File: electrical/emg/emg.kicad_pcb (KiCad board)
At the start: 2 copper layers, 257 parts, among them J1 USB_B, J10 Ref, J11 E2, J12 E1, J13 T1, J14 T2, J15 E2, J16 E1, J17 T1, J18 T2, J19 E2, J2 swd, J20 E1, J21 T1, J22 T2, J23 E2, J24 E1, J25 T1, J26 T2, J27 E2, J28 E1, J29 T1, J3 T3, J30 T2, J31 E2, J32 E1, J33 T1, J34 T2, J35 E2, J36 E1, J37 T1, J38 T2, J4 T3, J5 T3, J6 T3, J7 T3, J8 T3, J9 T3, P1 ~rst~, P2 bootldr, U1 stm32f405rgt6, U10 TSZ124IPT, U11 TSZ124IPT, U12 TSZ124IPT, U13 TSZ124IPT, U2 crystal-4pin, U3 my-NCP1117ST50T3G, U4 my-NCP1117ST50T3G, U5 TSV734IPT, U6 TSV734IPT, U7 TSZ124IPT, U8 TSZ124IPT, U9 TSZ124IPT

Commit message: a
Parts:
- moved R49 172.5 mm to (91.7, 133.7), turned to 180 degrees
- moved R53 170.2 mm to (103.2, 130.3)
- moved R48 168.9 mm to (91.9, 125.7), turned to 180 degrees
- moved R54 166.3 mm to (103.2, 128.5), turned to 180 degrees
- moved R51 165.7 mm to (95.2, 133.9)
- moved R41 164.4 mm to (83.2, 126.4), turned to 180 degrees
- moved R52 163.8 mm to (103.9, 124.3), turned to 270 degrees
- moved C35 160.6 mm to (87.6, 131.6), turned to 270 degrees
- moved R36 159.6 mm to (96.1, 111.3)
- moved R37 159.5 mm to (102.0, 110.3), turned to 270 degrees
- moved J17 159.1 mm to (99.6, 134.1)
- moved C37 158.8 mm to (100.9, 124.2)
- moved R42 157.9 mm to (83.2, 133.1), turned to 180 degrees
- moved R50 156.6 mm to (99.7, 122.4)
- moved R38 155.9 mm to (102.9, 107.7)
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
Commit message: a
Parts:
- added R260: 47k1%, Resistor_SMD:R_0603_1608Metric, F.Cu at (0.00, 0.00)
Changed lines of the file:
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@@
 (kicad_pcb (version 4) (host pcbnew 4.0.7-e2-6376~58~ubuntu16.04.1)
   (general
-    (links 475)
-    (no_connects 472)
-    (area 5.014286 -40.625 193.525001 124.961905)
+    (links 477)
+    (no_connects 474)
+    (area 0 0 0 0)
     (thickness 1.6)
     (drawings 0)
     (tracks 0)
     (zones 0)
-    (modules 257)
+    (modules 258)
     (nets 146)
   )
@@
       (net 1 GND))
   )
+  (module Resistor_SMD:R_0603_1608Metric (layer F.Cu)
+    (at 0 0)
+    (descr "Resistor SMD 0603 (1608 Metric), square (rectangular) end terminal, IPC_7351 nominal, (Body size source: http://www.tortai-tech.com/upload/download/2011102023233369053.pdf), generated with kicad-footprint-generator")
+    (tags resistor)
+    (attr smd)
+    (fp_text reference R260 (at 0 -1.65) (layer F.SilkS)
+      (effects (font (size 1 1) (thickness 0.15)))
+    )
+    (fp_text value 47k1% (at 0 1.65) (layer F.Fab)
+      (effects (font (size 1 1) (thickness 0.15)))
+    )
+    (fp_line (start -0.8 0.4) (end -0.8 -0.4) (layer F.Fab) (width 0.1))
+    (fp_line (start -0.8 -0.4) (end 0.8 -0.4) (layer F.Fab) (width 0.1))
+    (fp_line (start 0.8 -0.4) (end 0.8 0.4) (layer F.Fab) (width 0.1))
+    (fp_line (start 0.8 0.4) (end -0.8 0.4) (layer F.Fab) (width 0.1))
+    (fp_line (start -0.22 -0.51) (end 0.22 -0.51) (layer F.SilkS) (width 0.12))
+    (fp_line (start -0.22 0.51) (end 0.22 0.51) (layer F.SilkS) (width 0.12))
+    (fp_line (start -1.46 0.75) (end -1.46 -0.75) (layer F.CrtYd) (width 0.05))
+    (fp_line (start -1.46 -0.75) (end 1.46 -0.75) (layer F.CrtYd) (width 0.05))
+    (fp_line (start 1.46 -0.75) (end 1.46 0.75) (layer F.CrtYd) (width 0.05))
+    (fp_line (start 1.46 0.75) (end -1.46 0.75) (layer F.CrtYd) (width 0.05))
+    (fp_text user %R (at 0 0) (layer F.Fab)
+      (effects (font (size 0.5 0.5) (thickness 0.08)))
+    )
+    (pad 1 smd rect (at -0.875 0) (size 0.67 1) (layers F.Cu F.Paste F.Mask)
+      (net 4 GNDA))
+    (pad 2 smd rect (at 0.875 0) (size 0.67 1) (layers F.Cu F.Paste F.Mask)
+      (net 25 v_ref))
+    (model ${KISYS3DMOD}/Resistor_SMD.3dshapes/R_0603_1608Metric.wrl
+      (at (xyz 0 0 0))
+      (scale (xyz 1 1 1))
+      (rotate (xyz 0 0 0))
+    )
+  )
 )

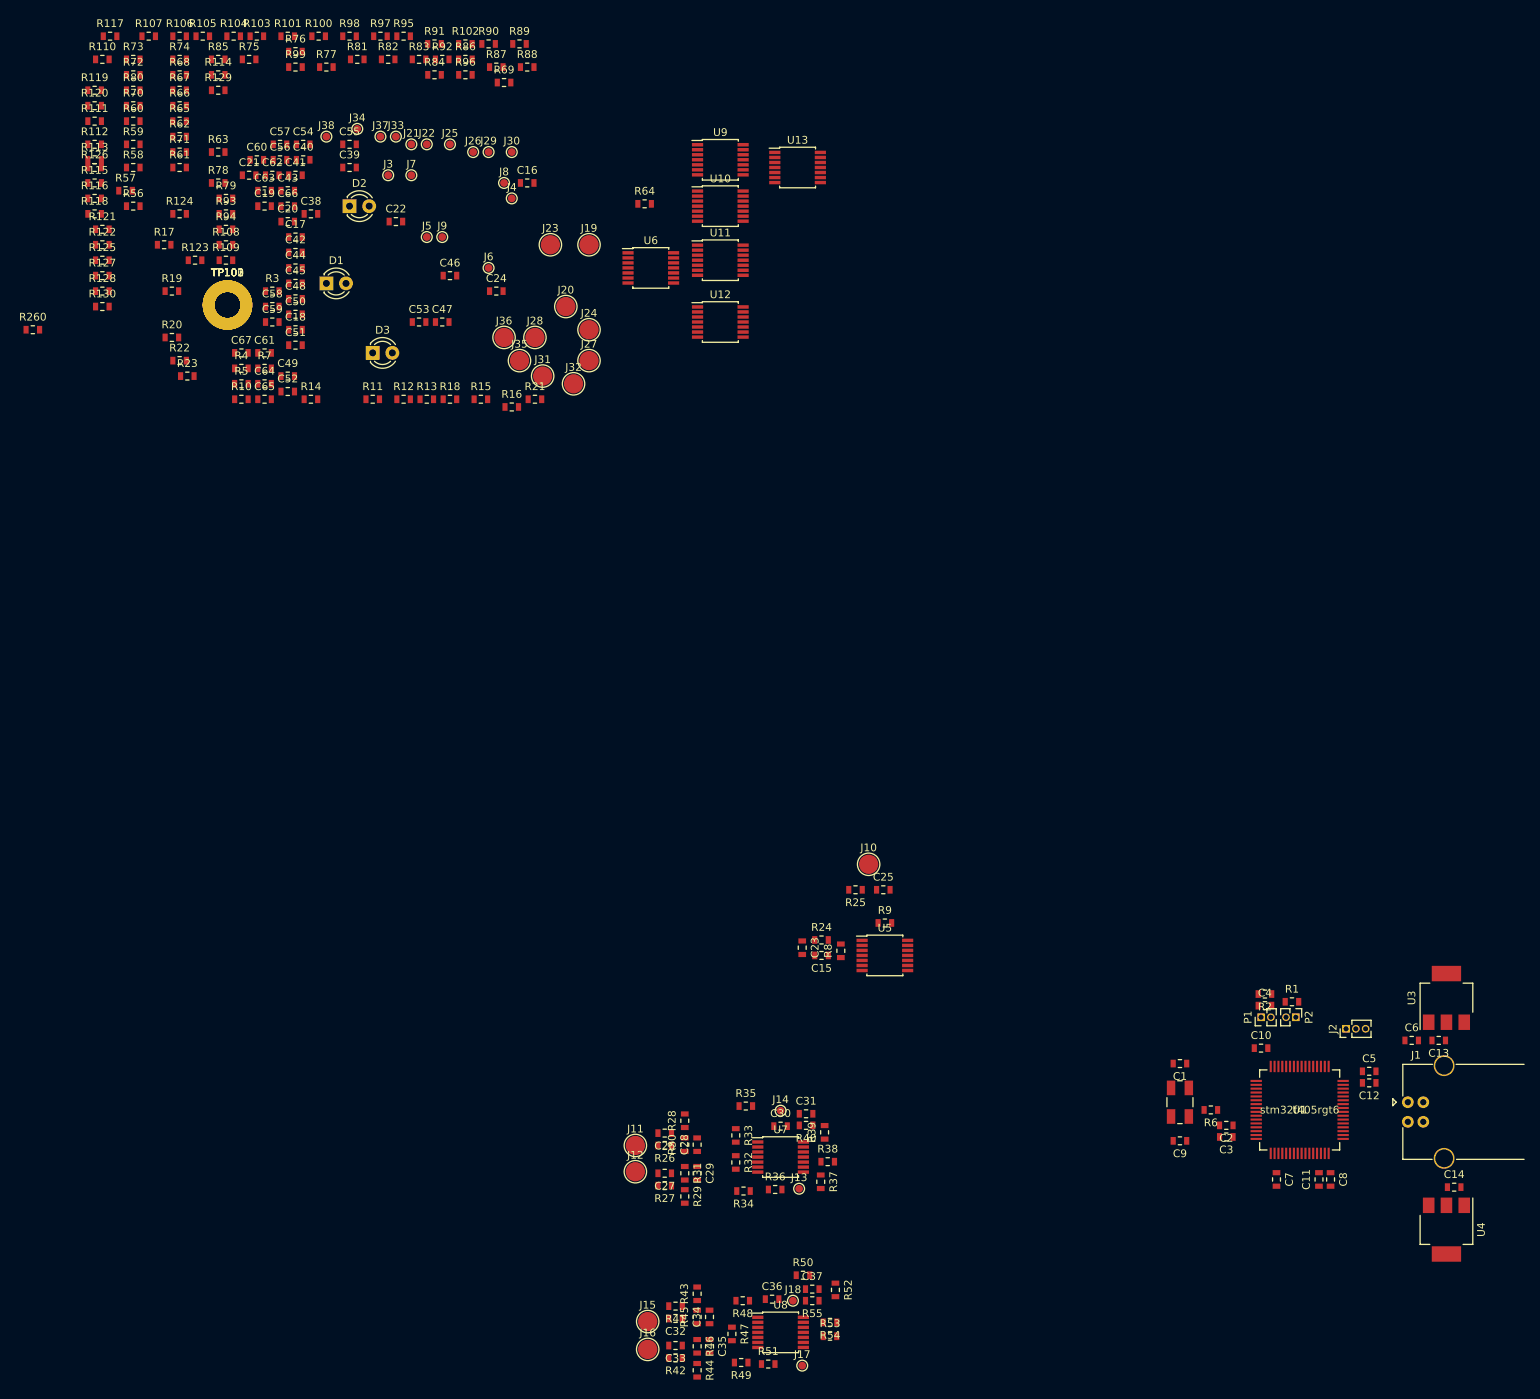
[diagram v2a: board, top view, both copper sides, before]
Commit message: Making two separate boards. One for ADC and the other one for preamplification.
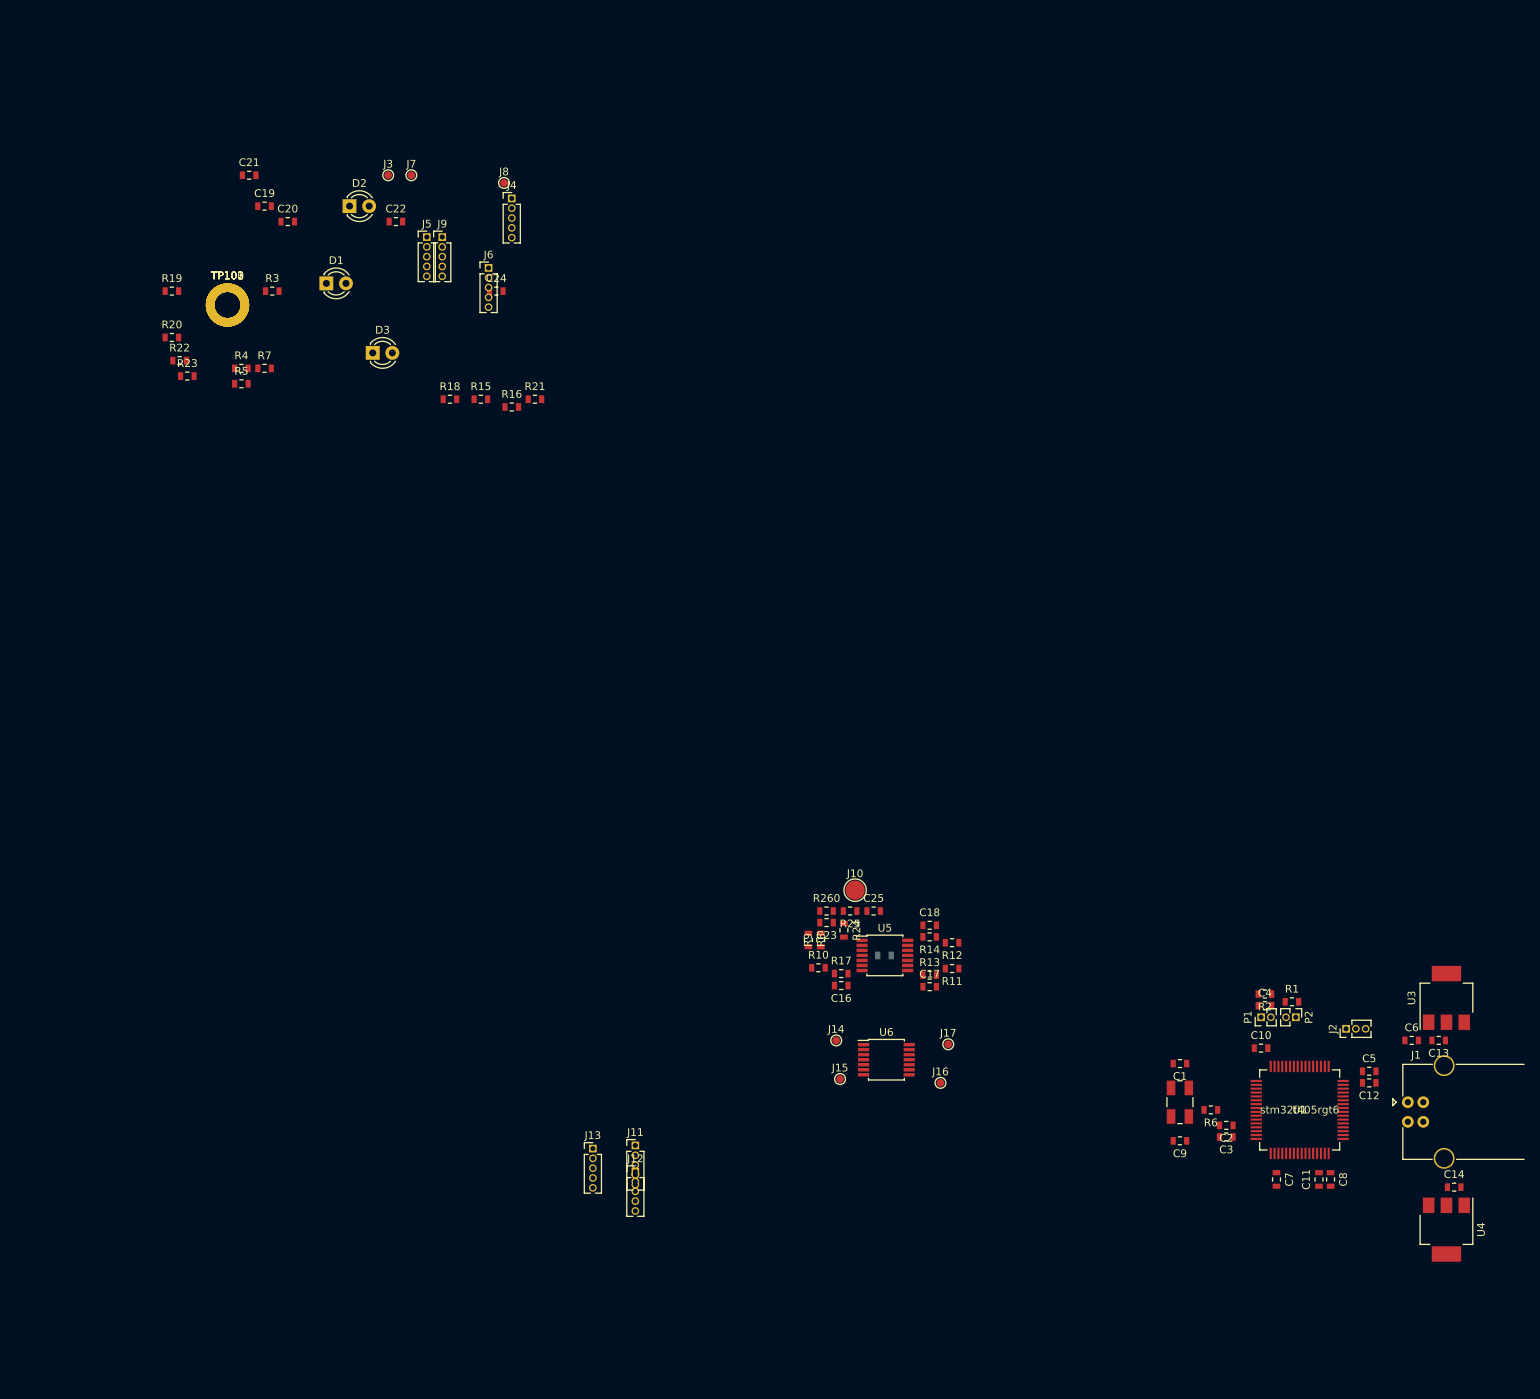
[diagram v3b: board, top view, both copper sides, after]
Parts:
- removed C26, C27, C32, C33, C38, C39, C44, C45, C50, C51, C56, C57, C62, C63: 22n, Capacitor_SMD:C_0603_1608Metric
- removed C28, C29, C31, C34, C35, C37, C40, C41, C43, C46, C47, C49, C52, C53, C55, C58, C59, C61, C64, C65, C67: 100n, Capacitor_SMD:C_0603_1608Metric
- removed C30, C36, C42, C48, C54, C60, C66: 2n2, Capacitor_SMD:C_0603_1608Metric
- removed J18, J22, J26, J30, J34, J38: T2, TestPoint:TestPoint_Pad_D1.0mm
- removed J19, J23, J27, J31, J35: E2, TestPoint:TestPoint_Pad_D2.5mm
- removed J20, J24, J28, J32, J36: E1, TestPoint:TestPoint_Pad_D2.5mm
- removed J21, J25, J29, J33, J37: T1, TestPoint:TestPoint_Pad_D1.0mm
- removed R100, R110, R111, R112, R113, R115, R125, R126, R127, R128, R130, R35, R36, R37, R38, R40, R50, R51, R52, R53, R55, R65, R66, R67, R68, R70, R80, R81, R82, R83, R85, R95, R96, R97, R98: 10k 1%, Resistor_SMD:R_0603_1608Metric
- removed R101, R102, R105, R106, R116, R117, R120, R121, R26, R27, R30, R31, R41, R42, R45, R46, R56, R57, R60, R61, R71, R72, R75, R76, R86, R87, R90, R91: 1k5 1%, Resistor_SMD:R_0603_1608Metric
- removed R103, R104, R118, R119, R28, R29, R43, R44, R58, R59, R73, R74, R88, R89: 1M 1%, Resistor_SMD:R_0603_1608Metric
- removed R107, R122, R32, R47, R62, R77, R92: 150 1%, Resistor_SMD:R_0603_1608Metric
- removed R108, R109, R123, R124, R33, R34, R48, R49, R63, R64, R78, R79, R93, R94: 47k1%, Resistor_SMD:R_0603_1608Metric
- removed R114, R129, R39, R54, R69, R84, R99: 1k 1%, Resistor_SMD:R_0603_1608Metric
- removed U10, U11, U12, U13, U7, U8, U9: TSZ124IPT, Package_SSOP:TSSOP-14_4.4x5mm_P0.65mm
- C15: moved to B.Cu
- C19: value 100n -> 2n2
- C24: value 2n2 -> 100n
- J11: value E2 -> Conn_01x05; footprint TestPoint:TestPoint_Pad_D2.5mm -> Pin_Headers:Pin_Header_Straight_1x05_Pitch1.27mm
- J12: value E1 -> Conn_01x05; footprint TestPoint:TestPoint_Pad_D2.5mm -> Pin_Headers:Pin_Header_Straight_1x05_Pitch1.27mm
- J13: value T1 -> Conn_01x05; footprint TestPoint:TestPoint_Pad_D1.0mm -> Pin_Headers:Pin_Header_Straight_1x05_Pitch1.27mm
- J14: value T2 -> T3
- J15: value E2 -> T3; footprint TestPoint:TestPoint_Pad_D2.5mm -> TestPoint:TestPoint_Pad_D1.0mm
- J16: value E1 -> T3; footprint TestPoint:TestPoint_Pad_D2.5mm -> TestPoint:TestPoint_Pad_D1.0mm
- J17: value T1 -> T3
- J4, J5, J6, J9: value T3 -> Conn_01x05; footprint TestPoint:TestPoint_Pad_D1.0mm -> Pin_Headers:Pin_Header_Straight_1x05_Pitch1.27mm
- R17, R18, R19, R20, R21, R22, R23: value 10k 1% -> 1k 1%
- TP100, TP101, TP102, TP103: footprint MountingHole:MountingHole_3.2mm_M3_Pad -> MountingHole:MountingHole_3.2mm_M3_DIN965_Pad
- moved R17 128.8 mm to (104.7, 83.3)
- moved R260 127.4 mm to (102.8, 75.2)
- moved C17 127.1 mm to (116.1, 85.0)
- moved C18 112.6 mm to (116.1, 77.1)
- moved C16 111.6 mm to (104.7, 84.9), turned to 180 degrees
- moved U6 106.9 mm to (110.5, 94.5)
- moved R14 106.1 mm to (116.1, 78.6), turned to 180 degrees
- moved R11 105.2 mm to (119.0, 82.7), turned to 180 degrees
- moved R10 104.9 mm to (101.7, 82.6)
- moved R12 100.0 mm to (119.0, 79.3), turned to 180 degrees
- moved R13 99.0 mm to (116.1, 83.5)
- moved J16 51.3 mm to (117.5, 97.5)
- moved J17 45.7 mm to (118.5, 92.5)
- moved J15 40.1 mm to (104.5, 97.0)
- moved J13 27.2 mm to (72.5, 106.0)
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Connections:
- C19 pad 1: /in_3 -> VDDA
- C19 pad 2: Net-(C19-Pad2) -> GNDA
- C20 pad 1: /in_4 -> /in_3
- C21 pad 1: /in_5 -> /in_4
- C22 pad 1: /in_6 -> /in_5
- C23 pad 1: v_ref -> /v_ref
- C24 pad 1: VDDA -> /in_6
- C24 pad 2: GNDA -> Net-(C24-Pad2)
- J11 pad 1: Net-(C26-Pad2) -> VDDA
- J12 pad 1: Net-(C27-Pad2) -> VDDA
- J13 pad 1: Net-(J13-Pad1) -> VDDA
- J14 pad 1: /inst_amp_0/out -> /in_3
- J15 pad 1: Net-(C32-Pad2) -> /in_4
- J16 pad 1: Net-(C33-Pad2) -> /in_5
- J17 pad 1: Net-(J17-Pad1) -> /in_6
- J4 pad 1: /in_1 -> VDDA
- J5 pad 1: /in_2 -> VDDA
- J6 pad 1: /in_3 -> VDDA
- J7 pad 1: /in_4 -> /in_1
- J8 pad 1: /in_5 -> /in_2
- J9 pad 1: /in_6 -> VDDA
- R10 pad 1: /inst_amp_0/out -> /v_ref
- R11 pad 1: /inst_amp_1/out -> /v_ref
- R12 pad 1: /inst_amp_2/out -> /v_ref
- R13 pad 1: /inst_amp_3/out -> Net-(C17-Pad2)
- R13 pad 2: Net-(C19-Pad2) -> /in_1
- R14 pad 1: /inst_amp_4/out -> Net-(C18-Pad2)
- R14 pad 2: Net-(C20-Pad2) -> /in_2
- R15 pad 1: /inst_amp_5/out -> /v_ref
- R15 pad 2: Net-(C21-Pad2) -> Net-(C20-Pad2)
- R16 pad 1: /inst_amp_6/out -> /v_ref
- R16 pad 2: Net-(C22-Pad2) -> Net-(C21-Pad2)
- R18 pad 1: Net-(C17-Pad2) -> /v_ref
- R18 pad 2: /in_1 -> Net-(C22-Pad2)
- R19 pad 1: Net-(C18-Pad2) -> /v_ref
- R19 pad 2: /in_2 -> Net-(C24-Pad2)
- R20 pad 1: Net-(C19-Pad2) -> Net-(C20-Pad2)
- R21 pad 1: Net-(C20-Pad2) -> Net-(C21-Pad2)
- R22 pad 1: Net-(C21-Pad2) -> Net-(C22-Pad2)
- R23 pad 1: Net-(C22-Pad2) -> Net-(C24-Pad2)
- R24 pad 1: v_ref -> /v_ref
- R25 pad 2: v_ref -> /v_ref
- R260 pad 2: v_ref -> /v_ref
- U5 pad 10: v_ref -> /v_1
- U5 pad 12: v_ref -> /v_2
- U5 pad 5: v_ref -> /v_0
- U6 pad 10: v_ref -> /v_5
- U6 pad 12: v_ref -> /v_6
- U6 pad 13: Net-(C22-Pad2) -> Net-(C24-Pad2)
- U6 pad 2: Net-(C19-Pad2) -> Net-(C20-Pad2)
- U6 pad 3: v_ref -> /v_3
- U6 pad 5: v_ref -> /v_4
- U6 pad 6: Net-(C20-Pad2) -> Net-(C21-Pad2)
- U6 pad 9: Net-(C21-Pad2) -> Net-(C22-Pad2)

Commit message: a
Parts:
- added R26: 100k 1%, Resistor_SMD:R_0603_1608Metric, F.Cu at (109.0, 85.8)
- added R27: 100k 1%, Resistor_SMD:R_0603_1608Metric, F.Cu at (111.2, 85.8)
- added R28: 100k 1%, Resistor_SMD:R_0603_1608Metric, F.Cu at (111.9, 76.1)
- added R29: 100k 1%, Resistor_SMD:R_0603_1608Metric, F.Cu at (107.0, 108.6)
- added R30: 100k 1%, Resistor_SMD:R_0603_1608Metric, F.Cu at (107.0, 118.4)
- added R31: 100k 1%, Resistor_SMD:R_0603_1608Metric, F.Cu at (109.8, 118.4)
- added R32: 100k 1%, Resistor_SMD:R_0603_1608Metric, F.Cu at (109.7, 108.6)
- moved C21 155.9 mm to (102.5, 116.9)
- moved R19 153.9 mm to (117.6, 112.3), turned to 180 degrees
- moved C22 147.3 mm to (114.5, 116.9), turned to 180 degrees
- moved R22 146.7 mm to (114.5, 115.3)
- moved R23 141.6 mm to (114.5, 111.5)
- moved C20 141.5 mm to (102.5, 109.2), turned to 180 degrees
- moved R20 138.6 mm to (102.5, 110.9)
- moved C24 127.1 mm to (114.5, 109.8), turned to 180 degrees
- moved R18 123.3 mm to (117.6, 114.6)
- moved J7 123.2 mm to (113.6, 84.9)
- moved J3 121.4 mm to (107.2, 84.9)
- moved R21 112.7 mm to (102.5, 115.3), turned to 180 degrees
- moved R16 111.2 mm to (99.3, 114.8)
- moved R15 110.8 mm to (99.3, 111.8)
- moved J8 109.6 mm to (113.7, 77.1)
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
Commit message: a
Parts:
- added R33: 1k 1%, Resistor_SMD:R_0603_1608Metric, F.Cu at (106.5, 90.1)
- added R34: 1k 1%, Resistor_SMD:R_0603_1608Metric, F.Cu at (114.9, 89.9)
- added R35: 1k 1%, Resistor_SMD:R_0603_1608Metric, F.Cu at (115.8, 71.5)
- added R36: 1k 1%, Resistor_SMD:R_0603_1608Metric, F.Cu at (105.9, 103.8)
- added R37: 1k 1%, Resistor_SMD:R_0603_1608Metric, F.Cu at (105.2, 125.3)
- added R38: 1k 1%, Resistor_SMD:R_0603_1608Metric, F.Cu at (111.8, 124.7)
- added R39: 1k 1%, Resistor_SMD:R_0603_1608Metric, F.Cu at (113.2, 103.8)
- C19: moved to B.Cu
- moved R7 186.1 mm to (183.3, 110.5)
- moved C19 151.5 mm to (108.5, 113.5)
- moved J9 131.5 mm to (69.7, 118.4)
- moved J4 82.9 mm to (92.5, 60.0)
- moved D2 82.0 mm to (48.6, 65.7)
- moved J5 75.4 mm to (76.8, 58.9)
- moved J6 72.6 mm to (85.5, 59.6)
- moved D1 66.8 mm to (48.5, 60.0)
- moved R3 66.4 mm to (45.0, 59.9)
- moved R4 63.3 mm to (45.0, 65.7)
- moved D3 50.8 mm to (48.3, 53.6)
- moved R5 50.0 mm to (44.9, 53.7)
- moved J13 21.8 mm to (72.5, 127.8)
- moved J12 19.4 mm to (82.0, 128.0)
- moved J11 14.7 mm to (78.4, 120.3)
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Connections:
- C16 pad 1: /in_0 -> Net-(C16-Pad1)
- C17 pad 1: /in_1 -> Net-(C17-Pad1)
- C18 pad 1: /in_2 -> Net-(C18-Pad1)
- C20 pad 1: /in_3 -> Net-(C20-Pad1)
- C21 pad 1: /in_4 -> Net-(C21-Pad1)
- C22 pad 1: /in_5 -> Net-(C22-Pad1)
- C24 pad 1: /in_6 -> Net-(C24-Pad1)
- J14 pad 1: /in_3 -> Net-(C20-Pad1)
- J15 pad 1: /in_4 -> Net-(C21-Pad1)
- J16 pad 1: /in_5 -> Net-(C22-Pad1)
- J17 pad 1: /in_6 -> Net-(C24-Pad1)
- J3 pad 1: /in_0 -> Net-(C16-Pad1)
- J7 pad 1: /in_1 -> Net-(C17-Pad1)
- J8 pad 1: /in_2 -> Net-(C18-Pad1)
- R13 pad 2: /in_1 -> Net-(C17-Pad1)
- R14 pad 2: /in_2 -> Net-(C18-Pad1)
- R17 pad 2: /in_0 -> Net-(C16-Pad1)
- R20 pad 2: /in_3 -> Net-(C20-Pad1)
- R21 pad 2: /in_4 -> Net-(C21-Pad1)
- R22 pad 2: /in_5 -> Net-(C22-Pad1)
- R23 pad 2: /in_6 -> Net-(C24-Pad1)
- R25 pad 2: /v_ref -> Net-(R24-Pad2)
- U5 pad 14: /in_2 -> Net-(C18-Pad1)
- U5 pad 7: /in_0 -> Net-(C16-Pad1)
- U5 pad 8: /in_1 -> Net-(C17-Pad1)
- U6 pad 1: /in_3 -> Net-(C20-Pad1)
- U6 pad 14: /in_6 -> Net-(C24-Pad1)
- U6 pad 7: /in_4 -> Net-(C21-Pad1)
- U6 pad 8: /in_5 -> Net-(C22-Pad1)

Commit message: a
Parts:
- added C26: 4u7, Capacitor_SMD:C_0603_1608Metric, F.Cu at (178.1, 114.2)
- R24: value 100 5% -> 10 5%
- moved TP100 184.1 mm to (183.0, 114.0)
- moved TP101 173.9 mm to (183.0, 87.0)
- moved TP103 158.3 mm to (123.0, 114.0)
- moved TP102 132.5 mm to (123.0, 87.0)
- moved R3 124.9 mm to (166.1, 90.1), turned to 90 degrees
- moved R4 121.9 mm to (164.5, 90.1), turned to 90 degrees
- moved D1 119.9 mm to (165.5, 86.0)
- moved R5 117.7 mm to (157.1, 89.4), turned to 180 degrees
- moved D2 116.3 mm to (163.1, 86.0), turned to 180 degrees
- moved D3 112.0 mm to (155.5, 86.0)
- moved J9 86.6 mm to (155.8, 108.7)
- moved J5 79.0 mm to (151.3, 85.1)
- moved J13 75.9 mm to (146.0, 108.7)
- moved J11 75.1 mm to (152.6, 108.7)
- moved J12 70.0 mm to (149.3, 108.7)
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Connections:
- R26 pad 2: /v_0 -> /v_2
- R28 pad 2: /v_2 -> /v_0
- R33 pad 2: /in_0 -> /in_2
- R35 pad 2: /in_2 -> /in_0
- TP100 pad 1: GND -> GNDA
- TP101 pad 1: GND -> GNDA
- TP102 pad 1: GND -> GNDA
- TP103 pad 1: GND -> GNDA
- U1 pad 26: /led-0 -> (no net)
- U1 pad 27: /led-1 -> (no net)
- U1 pad 28: /led-2 -> (no net)
- U1 pad 55: (no net) -> /led-0
- U1 pad 56: (no net) -> /led-1
- U1 pad 57: (no net) -> /led-2
- U5 pad 12: /v_2 -> /v_0
- U5 pad 5: /v_0 -> /v_2
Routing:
- net VDD: track 0.00 -> 37.2 mm
- net GND: track 0.00 -> 34.8 mm
- net /in_2: track 0.00 -> 32.1 mm
- net /in_0: track 0.00 -> 31.0 mm
- net /in_1: track 0.00 -> 21.8 mm
- net GNDA: track 0.00 -> 14.3 mm, vias 0 -> 2
- net /clk-in: track 0.00 -> 14.3 mm
- net /swd_io: track 0.00 -> 13.3 mm
- net /led-2: track 0.00 -> 11.8 mm
- net /~mcu-rst~: track 0.00 -> 11.3 mm, vias 0 -> 1
- net /dev_dp: track 0.00 -> 10.9 mm
- net /vbus: track 0.00 -> 10.4 mm
- net VDDA: track 0.00 -> 8.74 mm, vias 0 -> 2
- net /dev_dm: track 0.00 -> 8.67 mm
- net Net-(C20-Pad2): track 0.00 -> 8.32 mm
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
